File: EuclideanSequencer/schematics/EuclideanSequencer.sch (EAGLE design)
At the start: 47 parts, among them IC1 MEGA168, J1 AVR_SPI_PRG_6NS, Q1 2N3904, Q2 2N3904, Q3 2N3904, Q4 2N3904, Y1 16Mhz

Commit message: all panel components measured and locked
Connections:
- net N$13: now also CLKB.3; no longer CLKB.4
- net N$19: now also CLKIN.3, CLKTH.3; no longer CLKIN.4, CLKTH.4
- net N$26: now also CLKA.3; no longer CLKA.4
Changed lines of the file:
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@@
 <net name="N$19" class="0">
 <segment>
-<wire x1="-2.54" y1="-20.32" x2="5.08" y2="-20.32" width="0.1524" layer="91"/>
 <pinref part="R2" gate="G$1" pin="1"/>
-<wire x1="-2.54" y1="-40.64" x2="5.08" y2="-40.64" width="0.1524" layer="91"/>
 <wire x1="5.08" y1="-40.64" x2="10.16" y2="-40.64" width="0.1524" layer="91"/>
-<wire x1="5.08" y1="-20.32" x2="5.08" y2="-40.64" width="0.1524" layer="91"/>
-<junction x="5.08" y="-40.64"/>
-<pinref part="CLKTH" gate="G$1" pin="4"/>
-<pinref part="CLKIN" gate="G$1" pin="4"/>
+<wire x1="5.08" y1="-17.78" x2="5.08" y2="-38.1" width="0.1524" layer="91"/>
+<pinref part="CLKTH" gate="G$1" pin="3"/>
+<wire x1="5.08" y1="-38.1" x2="5.08" y2="-40.64" width="0.1524" layer="91"/>
+<wire x1="5.08" y1="-17.78" x2="-2.54" y2="-17.78" width="0.1524" layer="91"/>
+<pinref part="CLKIN" gate="G$1" pin="3"/>
+<wire x1="-2.54" y1="-38.1" x2="5.08" y2="-38.1" width="0.1524" layer="91"/>
+<junction x="5.08" y="-38.1"/>
 </segment>
 </net>
 <net name="N$13" class="0">
 <segment>
-<wire x1="139.7" y1="-35.56" x2="124.46" y2="-35.56" width="0.1524" layer="91"/>
 <pinref part="R" gate="G$1" pin="2"/>
-<wire x1="124.46" y1="-35.56" x2="124.46" y2="-40.64" width="0.1524" layer="91"/>
+<wire x1="124.46" y1="-33.02" x2="124.46" y2="-40.64" width="0.1524" layer="91"/>
 <pinref part="R11" gate="G$1" pin="2"/>
-<wire x1="124.46" y1="-35.56" x2="124.46" y2="-33.02" width="0.1524" layer="91"/>
-<junction x="124.46" y="-35.56"/>
-<pinref part="CLKB" gate="G$1" pin="4"/>
+<pinref part="CLKB" gate="G$1" pin="3"/>
+<wire x1="139.7" y1="-33.02" x2="124.46" y2="-33.02" width="0.1524" layer="91"/>
+<junction x="124.46" y="-33.02"/>
 </segment>
 </net>
@@
 <net name="N$26" class="0">
 <segment>
-<wire x1="248.92" y1="-35.56" x2="233.68" y2="-35.56" width="0.1524" layer="91"/>
 <pinref part="R7" gate="G$1" pin="2"/>
-<wire x1="233.68" y1="-35.56" x2="233.68" y2="-40.64" width="0.1524" layer="91"/>
+<wire x1="233.68" y1="-33.02" x2="233.68" y2="-40.64" width="0.1524" layer="91"/>
 <pinref part="R6" gate="G$1" pin="2"/>
-<wire x1="233.68" y1="-35.56" x2="233.68" y2="-33.02" width="0.1524" layer="91"/>
-<junction x="233.68" y="-35.56"/>
-<pinref part="CLKA" gate="G$1" pin="4"/>
+<pinref part="CLKA" gate="G$1" pin="3"/>
+<wire x1="248.92" y1="-33.02" x2="233.68" y2="-33.02" width="0.1524" layer="91"/>
+<junction x="233.68" y="-33.02"/>
 </segment>
 </net>

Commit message: a bit more routing
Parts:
- removed J1: AVR_SPI_PRG_6NS, SparkFun:AVR_SPI_PRG_6NS
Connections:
- removed net N$12: IC1.PB3(MOSI/OC2), J1.4
- net +5V: no longer J1.2
- net GND: no longer J1.6
- net N$11: no longer J1.3
- net N$31: no longer J1.5
- net N$9: no longer J1.1
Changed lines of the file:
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@@
 <grid distance="0.1" unitdist="inch" unit="inch" style="lines" multiple="1" display="no" altdistance="0.01" altunitdist="inch" altunit="inch"/>
 <layers>
-<layer number="1" name="Top" color="4" fill="1" visible="yes" active="no"/>
-<layer number="16" name="Bottom" color="1" fill="1" visible="yes" active="no"/>
-<layer number="17" name="Pads" color="2" fill="1" visible="yes" active="no"/>
-<layer number="18" name="Vias" color="2" fill="1" visible="yes" active="no"/>
-<layer number="19" name="Unrouted" color="6" fill="1" visible="yes" active="no"/>
-<layer number="20" name="Dimension" color="15" fill="1" visible="yes" active="no"/>
-<layer number="21" name="tPlace" color="7" fill="1" visible="yes" active="no"/>
-<layer number="22" name="bPlace" color="7" fill="1" visible="yes" active="no"/>
-<layer number="23" name="tOrigins" color="15" fill="1" visible="yes" active="no"/>
-<layer number="24" name="bOrigins" color="15" fill="1" visible="yes" active="no"/>
-<layer number="25" name="tNames" color="7" fill="1" visible="yes" active="no"/>
-<layer number="26" name="bNames" color="7" fill="1" visible="yes" active="no"/>
-<layer number="27" name="tValues" color="7" fill="1" visible="yes" active="no"/>
-<layer number="28" name="bValues" color="7" fill="1" visible="yes" active="no"/>
+<layer number="1" name="Top" color="4" fill="1" visible="no" active="no"/>
+<layer number="16" name="Bottom" color="1" fill="1" visible="no" active="no"/>
+<layer number="17" name="Pads" color="2" fill="1" visible="no" active="no"/>
+<layer number="18" name="Vias" color="2" fill="1" visible="no" active="no"/>
+<layer number="19" name="Unrouted" color="6" fill="1" visible="no" active="no"/>
+<layer number="20" name="Dimension" color="15" fill="1" visible="no" active="no"/>
+<layer number="21" name="tPlace" color="7" fill="1" visible="no" active="no"/>
+<layer number="22" name="bPlace" color="7" fill="1" visible="no" active="no"/>
+<layer number="23" name="tOrigins" color="15" fill="1" visible="no" active="no"/>
+<layer number="24" name="bOrigins" color="15" fill="1" visible="no" active="no"/>
+<layer number="25" name="tNames" color="7" fill="1" visible="no" active="no"/>
+<layer number="26" name="bNames" color="7" fill="1" visible="no" active="no"/>
+<layer number="27" name="tValues" color="7" fill="1" visible="no" active="no"/>
+<layer number="28" name="bValues" color="7" fill="1" visible="no" active="no"/>
 <layer number="29" name="tStop" color="7" fill="3" visible="no" active="no"/>
 <layer number="30" name="bStop" color="7" fill="6" visible="no" active="no"/>
@@
 <layer number="35" name="tGlue" color="7" fill="4" visible="no" active="no"/>
 <layer number="36" name="bGlue" color="7" fill="5" visible="no" active="no"/>
-<layer number="37" name="tTest" color="7" fill="1" visible="yes" active="no"/>
-<layer number="38" name="bTest" color="7" fill="1" visible="yes" active="no"/>
+<layer number="37" name="tTest" color="7" fill="1" visible="no" active="no"/>
+<layer number="38" name="bTest" color="7" fill="1" visible="no" active="no"/>
 <layer number="39" name="tKeepout" color="4" fill="11" visible="no" active="no"/>
 <layer number="40" name="bKeepout" color="1" fill="11" visible="no" active="no"/>
@@
 <layer number="44" name="Drills" color="7" fill="1" visible="no" active="no"/>
 <layer number="45" name="Holes" color="7" fill="1" visible="no" active="no"/>
-<layer number="46" name="Milling" color="3" fill="1" visible="yes" active="no"/>
-<layer number="47" name="Measures" color="7" fill="1" visible="yes" active="no"/>
-<layer number="48" name="Document" color="7" fill="1" visible="yes" active="no"/>
-<layer number="49" name="Reference" color="7" fill="1" visible="yes" active="no"/>
-<layer number="50" name="dxf" color="7" fill="1" visible="yes" active="no"/>
-<layer number="51" name="tDocu" color="7" fill="1" visible="yes" active="no"/>
-<layer number="52" name="bDocu" color="7" fill="1" visible="yes" active="no"/>
-<layer number="53" name="tGND_GNDA" color="7" fill="9" visible="yes" active="no"/>
-<layer number="54" name="bGND_GNDA" color="1" fill="9" visible="yes" active="no"/>
-<layer number="56" name="wert" color="7" fill="1" visible="yes" active="no"/>
+<layer number="46" name="Milling" color="3" fill="1" visible="no" active="no"/>
+<layer number="47" name="Measures" color="7" fill="1" visible="no" active="no"/>
+<layer number="48" name="Document" color="7" fill="1" visible="no" active="no"/>
+<layer number="49" name="Reference" color="7" fill="1" visible="no" active="no"/>
+<layer number="50" name="dxf" color="7" fill="1" visible="no" active="no"/>
+<layer number="51" name="tDocu" color="7" fill="1" visible="no" active="no"/>
+<layer number="52" name="bDocu" color="7" fill="1" visible="no" active="no"/>
+<layer number="53" name="tGND_GNDA" color="7" fill="9" visible="no" active="no"/>
+<layer number="54" name="bGND_GNDA" color="1" fill="9" visible="no" active="no"/>
+<layer number="56" name="wert" color="7" fill="1" visible="no" active="no"/>
 <layer number="91" name="Nets" color="15" fill="1" visible="yes" active="yes"/>
 <layer number="92" name="Busses" color="1" fill="1" visible="yes" active="yes"/>
@@
 <part name="Y1" library="SparkFun" deviceset="RESONATOR" device="PTH" value="16Mhz"/>
 <part name="P+7" library="supply1" deviceset="+5V" device=""/>
-<part name="J1" library="SparkFun" deviceset="AVR_SPI_PRG_6" device="NS"/>
-<part name="P+8" library="supply1" deviceset="+5V" device=""/>
-<part name="GND8" library="supply1" deviceset="GND" device=""/>
 <part name="C3" library="rcl" deviceset="C-US" device="050-024X044" value="100n"/>
 <part name="GND9" library="supply1" deviceset="GND" device=""/>
@@
 <instance part="Y1" gate="G$1" x="22.86" y="53.34" rot="R270"/>
 <instance part="P+7" gate="1" x="27.94" y="83.82"/>
-<instance part="J1" gate="G$1" x="109.22" y="15.24"/>
-<instance part="P+8" gate="1" x="127" y="25.4" smashed="yes">
-<attribute name="VALUE" x="127" y="27.94" size="1.778" layer="96" rot="R180"/>
-</instance>
-<instance part="GND8" gate="1" x="127" y="5.08"/>
 <instance part="C3" gate="G$1" x="27.94" y="27.94"/>
 <instance part="GND9" gate="1" x="12.7" y="15.24"/>
@@
 </segment>
 <segment>
-<pinref part="J1" gate="G$1" pin="2"/>
-<wire x1="119.38" y1="17.78" x2="127" y2="17.78" width="0.1524" layer="91"/>
-<pinref part="P+8" gate="1" pin="+5V"/>
-<wire x1="127" y1="17.78" x2="127" y2="22.86" width="0.1524" layer="91"/>
-</segment>
-<segment>
 <pinref part="P+12" gate="1" pin="+5V"/>
 <wire x1="254" y1="86.36" x2="254" y2="76.2" width="0.1524" layer="91"/>
@@
 <pinref part="ROTA" gate="G$1" pin="2"/>
 <wire x1="205.74" y1="86.36" x2="208.28" y2="86.36" width="0.1524" layer="91"/>
-</segment>
-<segment>
-<pinref part="J1" gate="G$1" pin="6"/>
-<wire x1="119.38" y1="12.7" x2="127" y2="12.7" width="0.1524" layer="91"/>
-<pinref part="GND8" gate="1" pin="GND"/>
-<wire x1="127" y1="12.7" x2="127" y2="7.62" width="0.1524" layer="91"/>
 </segment>
 <segment>
@@
 <net name="N$9" class="0">
 <segment>
-<pinref part="J1" gate="G$1" pin="1"/>
 <pinref part="IC1" gate="G$1" pin="PB4(MISO)"/>
-<wire x1="101.6" y1="17.78" x2="86.36" y2="17.78" width="0.1524" layer="91"/>
 <pinref part="LED2" gate="G$1" pin="A"/>
 <wire x1="86.36" y1="17.78" x2="81.28" y2="17.78" width="0.1524" layer="91"/>
 <wire x1="86.36" y1="10.16" x2="86.36" y2="17.78" width="0.1524" layer="91"/>
-<junction x="86.36" y="17.78"/>
 </segment>
 </net>
@@
 <pinref part="IC1" gate="G$1" pin="PB5(SCK)"/>
 <wire x1="81.28" y1="15.24" x2="93.98" y2="15.24" width="0.1524" layer="91"/>
-<pinref part="J1" gate="G$1" pin="3"/>
 <pinref part="LED3" gate="G$1" pin="A"/>
-<wire x1="93.98" y1="15.24" x2="101.6" y2="15.24" width="0.1524" layer="91"/>
 <wire x1="93.98" y1="10.16" x2="93.98" y2="15.24" width="0.1524" layer="91"/>
-<junction x="93.98" y="15.24"/>
-</segment>
-</net>
-<net name="N$12" class="0">
-<segment>
-<pinref part="J1" gate="G$1" pin="4"/>
-<wire x1="119.38" y1="15.24" x2="124.46" y2="15.24" width="0.1524" layer="91"/>
-<wire x1="124.46" y1="15.24" x2="124.46" y2="22.86" width="0.1524" layer="91"/>
-<wire x1="124.46" y1="22.86" x2="101.6" y2="22.86" width="0.1524" layer="91"/>
-<wire x1="101.6" y1="22.86" x2="101.6" y2="20.32" width="0.1524" layer="91"/>
-<pinref part="IC1" gate="G$1" pin="PB3(MOSI/OC2)"/>
-<wire x1="101.6" y1="20.32" x2="81.28" y2="20.32" width="0.1524" layer="91"/>
 </segment>
 </net>
@@
 <net name="N$31" class="0">
 <segment>
-<pinref part="J1" gate="G$1" pin="5"/>
-<wire x1="101.6" y1="12.7" x2="101.6" y2="-15.24" width="0.1524" layer="91"/>
-<wire x1="101.6" y1="-15.24" x2="68.58" y2="-15.24" width="0.1524" layer="91"/>
-<wire x1="68.58" y1="-15.24" x2="68.58" y2="5.08" width="0.1524" layer="91"/>
-<wire x1="-2.54" y1="5.08" x2="-2.54" y2="73.66" width="0.1524" layer="91"/>
 <pinref part="IC1" gate="G$1" pin="PC6(/RESET)"/>
 <wire x1="-2.54" y1="73.66" x2="15.24" y2="73.66" width="0.1524" layer="91"/>
@@
 <wire x1="15.24" y1="73.66" x2="33.02" y2="73.66" width="0.1524" layer="91"/>
 <wire x1="-2.54" y1="73.66" x2="-2.54" y2="78.74" width="0.1524" layer="91"/>
-<junction x="-2.54" y="73.66"/>
 <pinref part="R3" gate="G$1" pin="1"/>
 <wire x1="15.24" y1="73.66" x2="15.24" y2="78.74" width="0.1524" layer="91"/>
 <junction x="15.24" y="73.66"/>
-<wire x1="68.58" y1="5.08" x2="-2.54" y2="5.08" width="0.1524" layer="91"/>
-</segment>
-</net>
+</segment>
+</net>

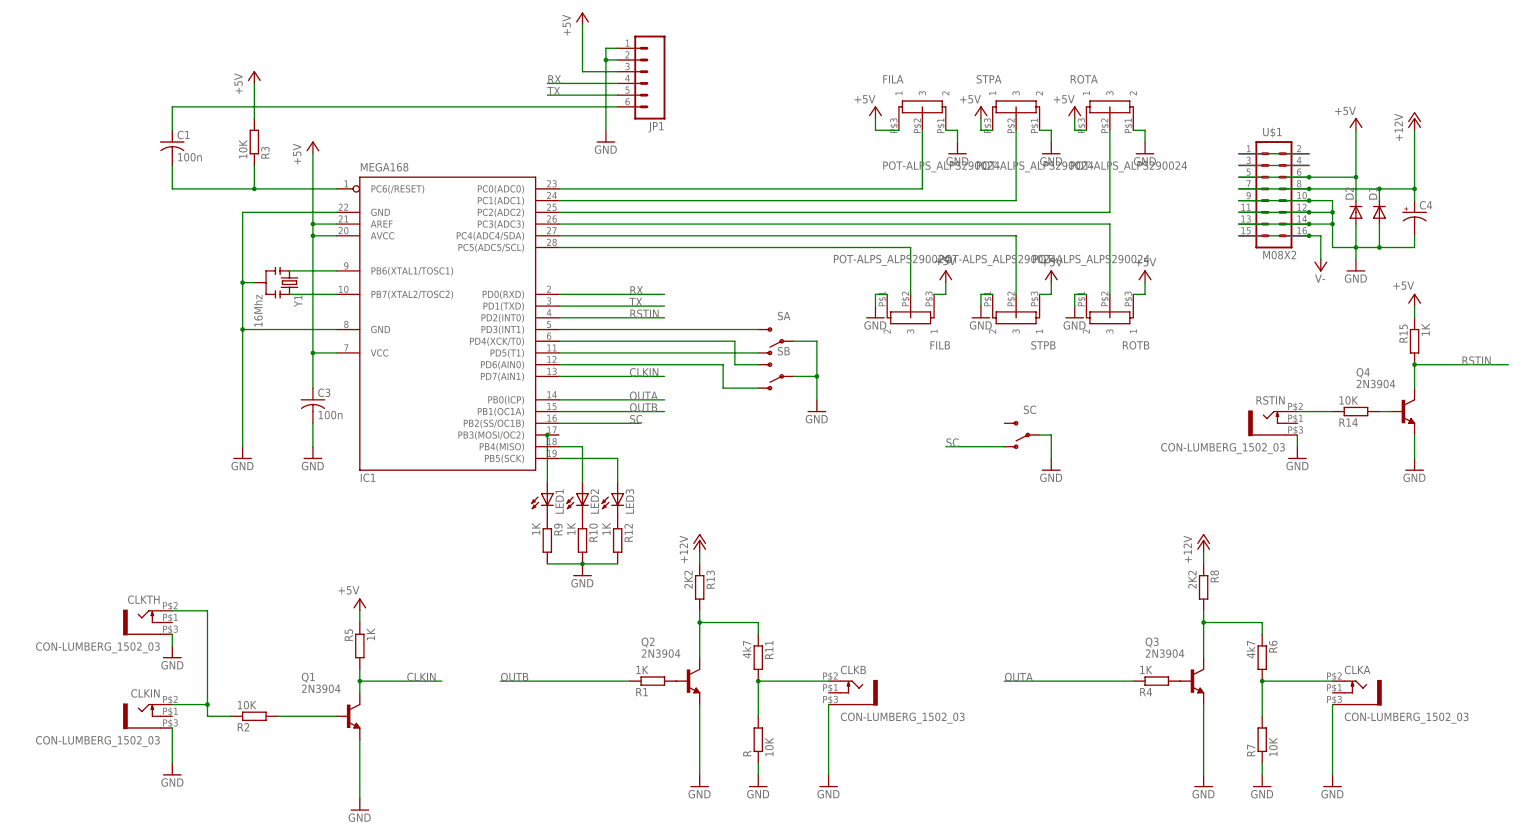
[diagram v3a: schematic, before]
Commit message: Moved clock input to INT1. Added reset function to switch C. Re-arranged switch pins. Turned power header around. Fixed LED1 net. Moved CLKTH on board.
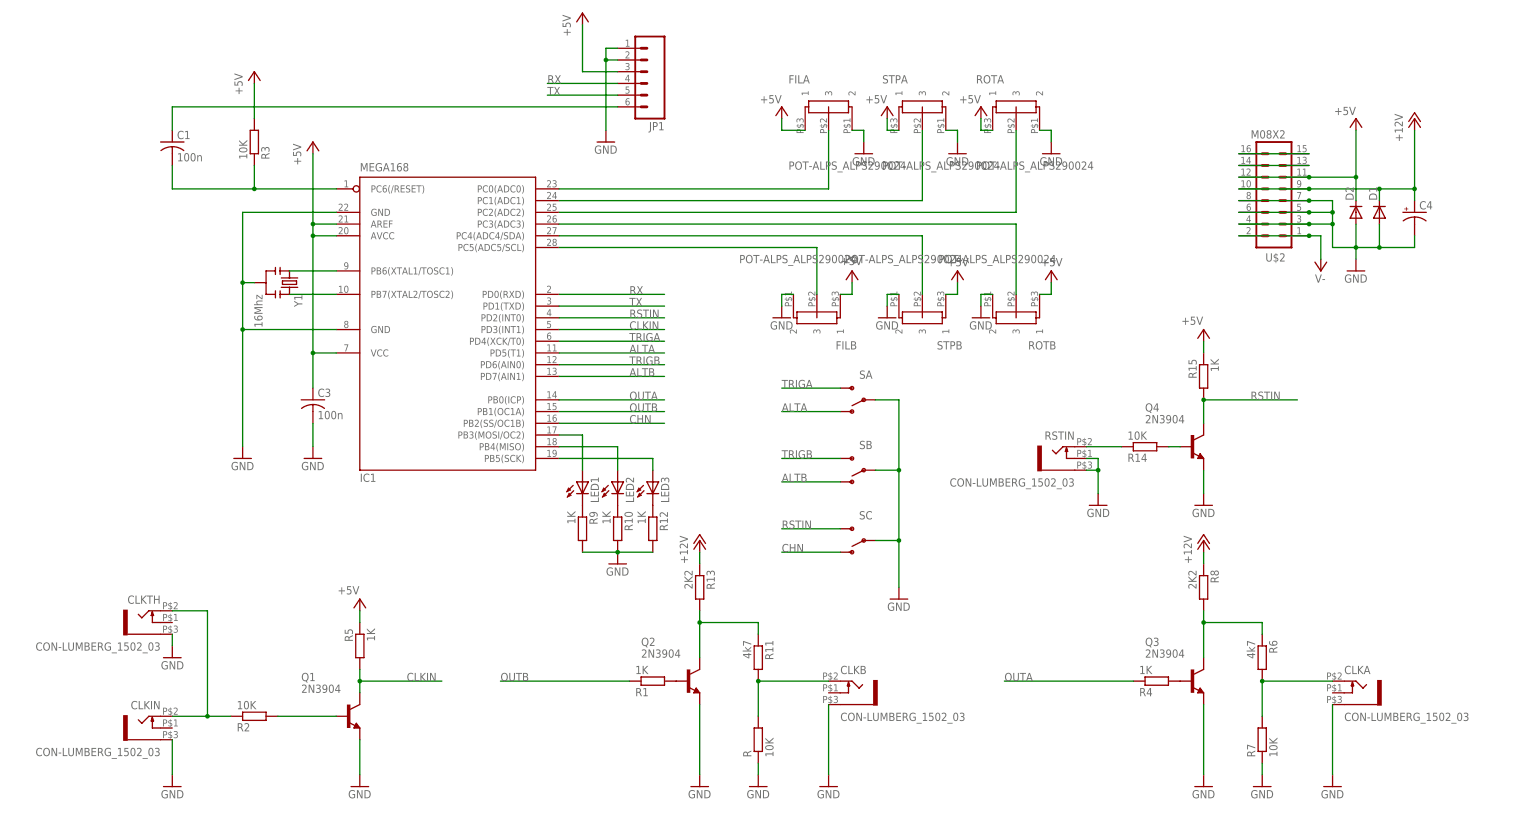
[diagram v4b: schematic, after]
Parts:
- removed U$1: M08X2, SparkFun:M08X2
- added U$2: M08X2, SparkFun:M08X2
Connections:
- net N$10 renamed ALTA
- net SC renamed CHN
- removed net N$15: IC1.PD3(INT1), SA.S
- removed net N$16: LED1.A
- removed net N$22: IC1.PD4(XCK/T0), SB.S
- removed net N$23: IC1.PD6(AIN0), SB.O
- new net ALTB: IC1.PD7(AIN1), SB.O
- new net N$12: IC1.PB3(MOSI/OC2), LED1.A
- new net TRIGA: IC1.PD4(XCK/T0), SA.S
- new net TRIGB: IC1.PD6(AIN0), SB.S
- net +12V: now also U$2.10, U$2.9; no longer U$1.7, U$1.8
- net +5V: now also U$2.11, U$2.12; no longer U$1.5, U$1.6
- net CLKIN: now also IC1.PD3(INT1); no longer IC1.PD7(AIN1)
- net GND: now also RSTIN.4, U$2.3, U$2.4, U$2.5, U$2.6, U$2.7, U$2.8; no longer U$1.10, U$1.11, U$1.12, U$1.13, U$1.14, U$1.9
- net N$18: now also U$2.13, U$2.14; no longer U$1.3, U$1.4
- net PWR_BUS: now also U$2.15, U$2.16; no longer U$1.1, U$1.2
- net RSTIN: now also SC.S
- net V-: now also U$2.1, U$2.2; no longer U$1.15, U$1.16
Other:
- moved on the sheet: CLKIN, FILA, FILB, LED1, LED2, LED3, Q4, R10, R12, R14, R15, R9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
